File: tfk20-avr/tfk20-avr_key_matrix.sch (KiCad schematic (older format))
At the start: 42 parts

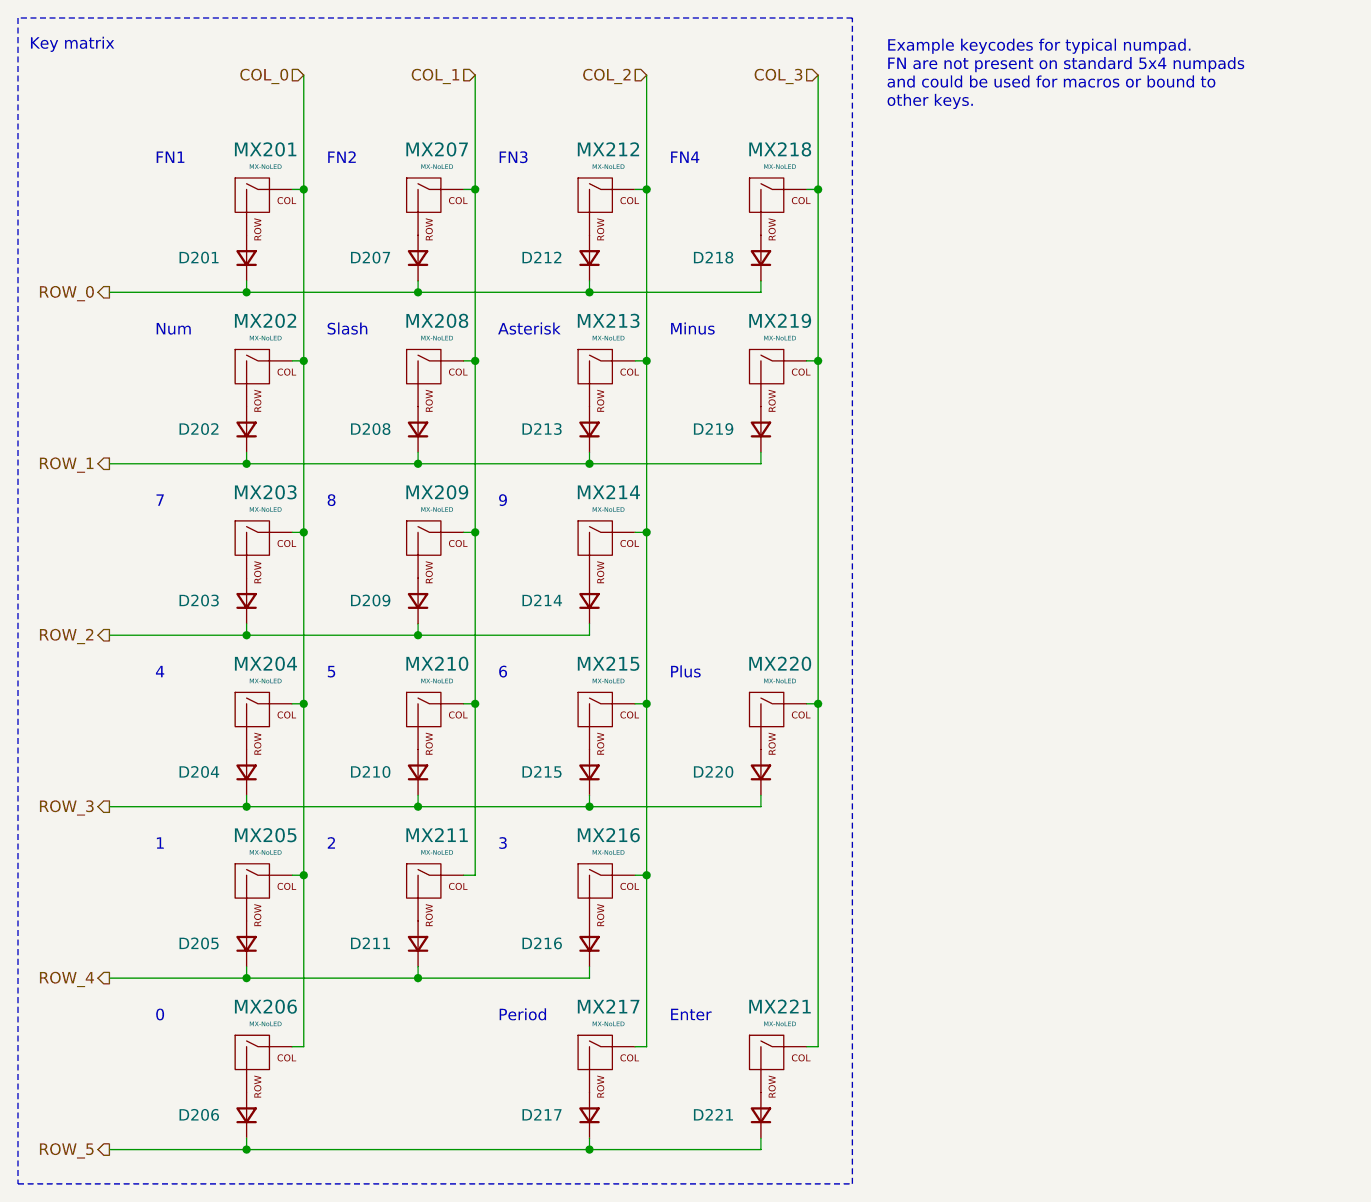
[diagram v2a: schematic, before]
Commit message: Add ISP header
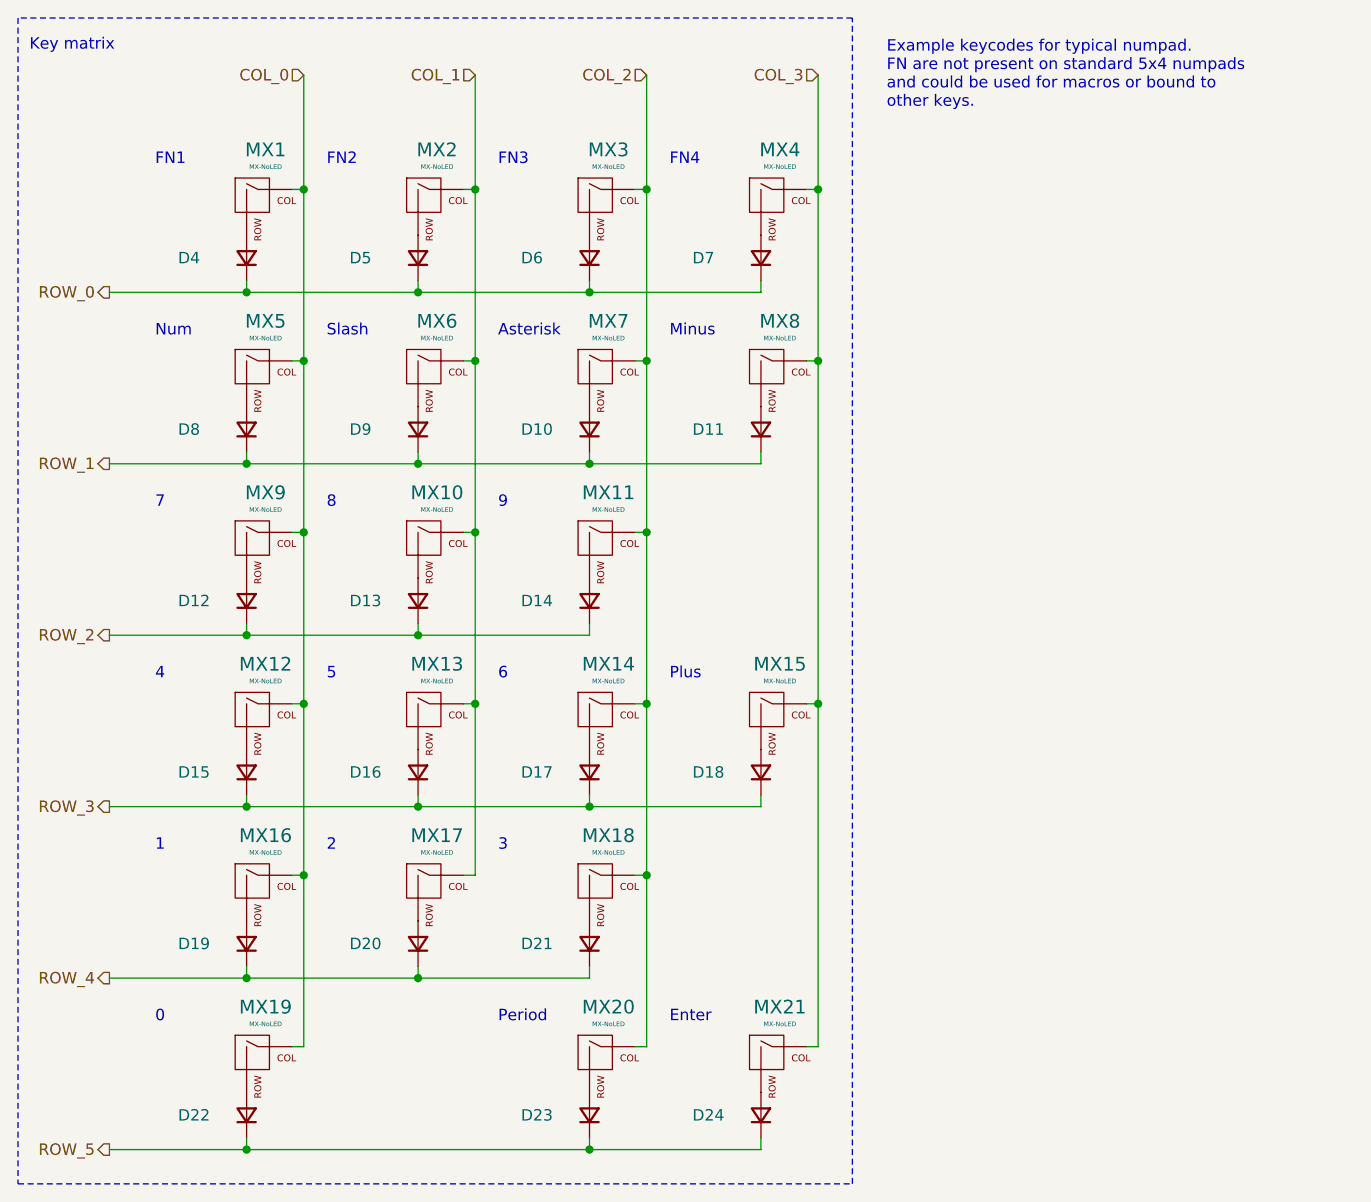
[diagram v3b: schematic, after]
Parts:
- renumbered D213 to D10, D219 to D11, D203 to D12, D209 to D13, D214 to D14, D204 to D15, D210 to D16, D215 to D17, D220 to D18, D205 to D19, D211 to D20, D216 to D21, D206 to D22, D217 to D23, D221 to D24, D201 to D4, D207 to D5, D212 to D6, D218 to D7, D202 to D8, D208 to D9, MX201 to MX1, MX209 to MX10, MX214 to MX11, MX204 to MX12, MX210 to MX13, MX215 to MX14, MX220 to MX15, MX205 to MX16, MX211 to MX17, MX216 to MX18, MX206 to MX19, MX207 to MX2, MX217 to MX20, MX221 to MX21, MX212 to MX3, MX218 to MX4, MX202 to MX5, MX208 to MX6, MX213 to MX7, MX219 to MX8, MX203 to MX9

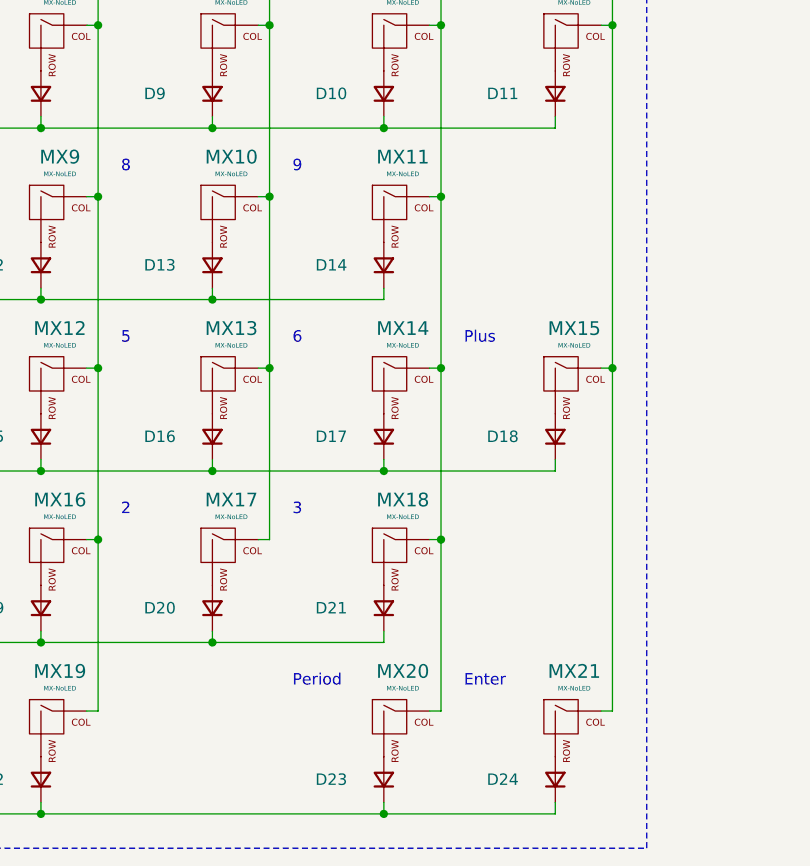
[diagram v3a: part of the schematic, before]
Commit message: Assign some footprints
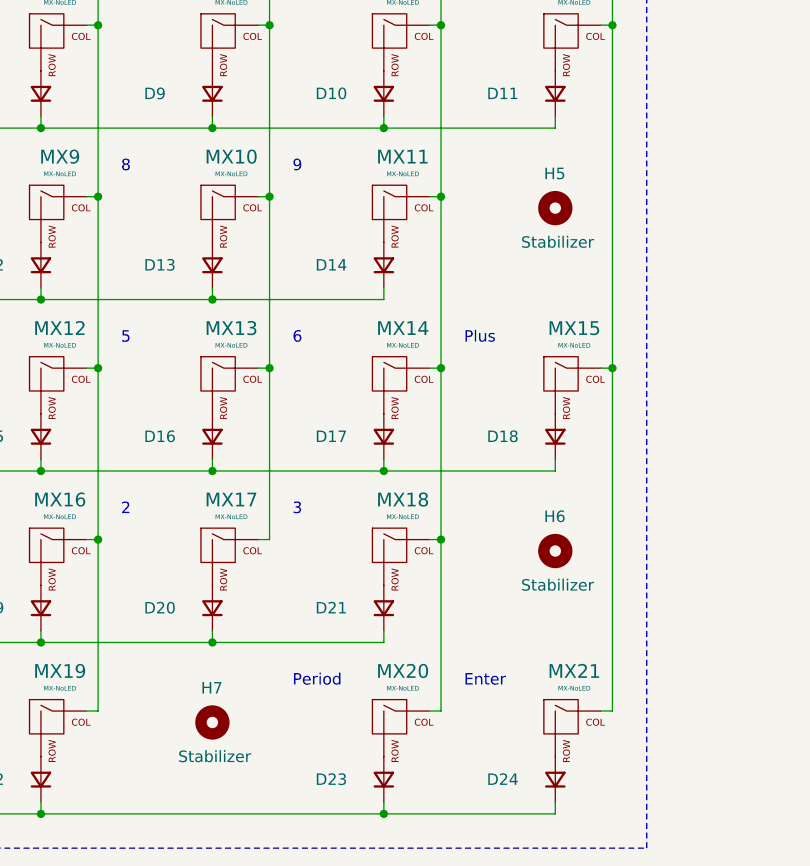
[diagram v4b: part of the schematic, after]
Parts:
- added H5, H6, H7: Stabilizer, Mounting_Keyboard_Stabilizer:Stabilizer_Cherry_MX_2u, symbol Mechanical:MountingHole
- D10, D11, D12, D13, D14, D15, D16, D17, D18, D19, D20, D21, D22, D23, D24, D4, D5, D6, D7, D8, D9: value D_Small -> Switch diode; footprint (none) -> Diode_SMD:D_SOD-123
- MX1, MX10, MX11, MX12, MX13, MX14, MX16, MX17, MX18, MX2, MX20, MX3, MX4, MX5, MX6, MX7, MX8, MX9: footprint (none) -> Switch_Keyboard_Kailh:SW_Hotswap_Kailh_1.00u
- MX15, MX19, MX21: footprint (none) -> Switch_Keyboard_Kailh:SW_Hotswap_Kailh_2.00u

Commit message: Remove alternative LEDs
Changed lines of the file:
@@
 P 4650 2550
 F 0 "MX5" H 4683 2773 60  0000 C CNN
-F 1 "MX-NoLED" H 4683 2699 20  0000 C CNN
+F 1 "MX-NoLED" H 4683 2699 20  0001 C CNN
 F 2 "Switch_Keyboard_Kailh:SW_Hotswap_Kailh_1.00u" H 4025 2525 60  0001 C CNN
 F 3 "" H 4025 2525 60  0001 C CNN
@@
 P 4650 3300
 F 0 "MX9" H 4683 3523 60  0000 C CNN
-F 1 "MX-NoLED" H 4683 3449 20  0000 C CNN
+F 1 "MX-NoLED" H 4683 3449 20  0001 C CNN
 F 2 "Switch_Keyboard_Kailh:SW_Hotswap_Kailh_1.00u" H 4025 3275 60  0001 C CNN
 F 3 "" H 4025 3275 60  0001 C CNN
@@
 P 5400 2550
 F 0 "MX6" H 5433 2773 60  0000 C CNN
-F 1 "MX-NoLED" H 5433 2699 20  0000 C CNN
+F 1 "MX-NoLED" H 5433 2699 20  0001 C CNN
 F 2 "Switch_Keyboard_Kailh:SW_Hotswap_Kailh_1.00u" H 4775 2525 60  0001 C CNN
 F 3 "" H 4775 2525 60  0001 C CNN
@@
 P 5400 3300
 F 0 "MX10" H 5433 3523 60  0000 C CNN
-F 1 "MX-NoLED" H 5433 3449 20  0000 C CNN
+F 1 "MX-NoLED" H 5433 3449 20  0001 C CNN
 F 2 "Switch_Keyboard_Kailh:SW_Hotswap_Kailh_1.00u" H 4775 3275 60  0001 C CNN
 F 3 "" H 4775 3275 60  0001 C CNN
@@
 P 6150 2550
 F 0 "MX7" H 6183 2773 60  0000 C CNN
-F 1 "MX-NoLED" H 6183 2699 20  0000 C CNN
+F 1 "MX-NoLED" H 6183 2699 20  0001 C CNN
 F 2 "Switch_Keyboard_Kailh:SW_Hotswap_Kailh_1.00u" H 5525 2525 60  0001 C CNN
 F 3 "" H 5525 2525 60  0001 C CNN
@@
 P 6150 3300
 F 0 "MX11" H 6183 3523 60  0000 C CNN
-F 1 "MX-NoLED" H 6183 3449 20  0000 C CNN
+F 1 "MX-NoLED" H 6183 3449 20  0001 C CNN
 F 2 "Switch_Keyboard_Kailh:SW_Hotswap_Kailh_1.00u" H 5525 3275 60  0001 C CNN
 F 3 "" H 5525 3275 60  0001 C CNN
@@
 P 6900 2550
 F 0 "MX8" H 6933 2773 60  0000 C CNN
-F 1 "MX-NoLED" H 6933 2699 20  0000 C CNN
+F 1 "MX-NoLED" H 6933 2699 20  0001 C CNN
 F 2 "Switch_Keyboard_Kailh:SW_Hotswap_Kailh_1.00u" H 6275 2525 60  0001 C CNN
 F 3 "" H 6275 2525 60  0001 C CNN
@@
 P 4650 4050
 F 0 "MX12" H 4683 4273 60  0000 C CNN
-F 1 "MX-NoLED" H 4683 4199 20  0000 C CNN
+F 1 "MX-NoLED" H 4683 4199 20  0001 C CNN
 F 2 "Switch_Keyboard_Kailh:SW_Hotswap_Kailh_1.00u" H 4025 4025 60  0001 C CNN
 F 3 "" H 4025 4025 60  0001 C CNN
@@
 P 5400 4050
 F 0 "MX13" H 5433 4273 60  0000 C CNN
-F 1 "MX-NoLED" H 5433 4199 20  0000 C CNN
+F 1 "MX-NoLED" H 5433 4199 20  0001 C CNN
 F 2 "Switch_Keyboard_Kailh:SW_Hotswap_Kailh_1.00u" H 4775 4025 60  0001 C CNN
 F 3 "" H 4775 4025 60  0001 C CNN
@@
 P 6150 4050
 F 0 "MX14" H 6183 4273 60  0000 C CNN
-F 1 "MX-NoLED" H 6183 4199 20  0000 C CNN
+F 1 "MX-NoLED" H 6183 4199 20  0001 C CNN
 F 2 "Switch_Keyboard_Kailh:SW_Hotswap_Kailh_1.00u" H 5525 4025 60  0001 C CNN
 F 3 "" H 5525 4025 60  0001 C CNN
@@
 P 6900 4050
 F 0 "MX15" H 6933 4273 60  0000 C CNN
-F 1 "MX-NoLED" H 6933 4199 20  0000 C CNN
+F 1 "MX-NoLED" H 6933 4199 20  0001 C CNN
 F 2 "Switch_Keyboard_Kailh:SW_Hotswap_Kailh_2.00u" H 6275 4025 60  0001 C CNN
 F 3 "" H 6275 4025 60  0001 C CNN
@@
 P 4650 4800
 F 0 "MX16" H 4683 5023 60  0000 C CNN
-F 1 "MX-NoLED" H 4683 4949 20  0000 C CNN
+F 1 "MX-NoLED" H 4683 4949 20  0001 C CNN
 F 2 "Switch_Keyboard_Kailh:SW_Hotswap_Kailh_1.00u" H 4025 4775 60  0001 C CNN
 F 3 "" H 4025 4775 60  0001 C CNN
@@
 P 5400 4800
 F 0 "MX17" H 5433 5023 60  0000 C CNN
-F 1 "MX-NoLED" H 5433 4949 20  0000 C CNN
+F 1 "MX-NoLED" H 5433 4949 20  0001 C CNN
 F 2 "Switch_Keyboard_Kailh:SW_Hotswap_Kailh_1.00u" H 4775 4775 60  0001 C CNN
 F 3 "" H 4775 4775 60  0001 C CNN
@@
 P 6150 4800
 F 0 "MX18" H 6183 5023 60  0000 C CNN
-F 1 "MX-NoLED" H 6183 4949 20  0000 C CNN
+F 1 "MX-NoLED" H 6183 4949 20  0001 C CNN
 F 2 "Switch_Keyboard_Kailh:SW_Hotswap_Kailh_1.00u" H 5525 4775 60  0001 C CNN
 F 3 "" H 5525 4775 60  0001 C CNN
@@
 P 4650 5550
 F 0 "MX19" H 4683 5773 60  0000 C CNN
-F 1 "MX-NoLED" H 4683 5699 20  0000 C CNN
+F 1 "MX-NoLED" H 4683 5699 20  0001 C CNN
 F 2 "Switch_Keyboard_Kailh:SW_Hotswap_Kailh_2.00u" H 4025 5525 60  0001 C CNN
 F 3 "" H 4025 5525 60  0001 C CNN
@@
 P 6150 5550
 F 0 "MX20" H 6183 5773 60  0000 C CNN
-F 1 "MX-NoLED" H 6183 5699 20  0000 C CNN
+F 1 "MX-NoLED" H 6183 5699 20  0001 C CNN
 F 2 "Switch_Keyboard_Kailh:SW_Hotswap_Kailh_1.00u" H 5525 5525 60  0001 C CNN
 F 3 "" H 5525 5525 60  0001 C CNN
@@
 P 6900 5550
 F 0 "MX21" H 6933 5773 60  0000 C CNN
-F 1 "MX-NoLED" H 6933 5699 20  0000 C CNN
+F 1 "MX-NoLED" H 6933 5699 20  0001 C CNN
 F 2 "Switch_Keyboard_Kailh:SW_Hotswap_Kailh_2.00u" H 6275 5525 60  0001 C CNN
 F 3 "" H 6275 5525 60  0001 C CNN
@@
 P 4650 1800
 F 0 "MX1" H 4683 2023 60  0000 C CNN
-F 1 "MX-NoLED" H 4683 1949 20  0000 C CNN
+F 1 "MX-NoLED" H 4683 1949 20  0001 C CNN
 F 2 "Switch_Keyboard_Kailh:SW_Hotswap_Kailh_1.00u" H 4025 1775 60  0001 C CNN
 F 3 "" H 4025 1775 60  0001 C CNN
@@
 P 5400 1800
 F 0 "MX2" H 5433 2023 60  0000 C CNN
-F 1 "MX-NoLED" H 5433 1949 20  0000 C CNN
+F 1 "MX-NoLED" H 5433 1949 20  0001 C CNN
 F 2 "Switch_Keyboard_Kailh:SW_Hotswap_Kailh_1.00u" H 4775 1775 60  0001 C CNN
 F 3 "" H 4775 1775 60  0001 C CNN
@@
 P 6150 1800
 F 0 "MX3" H 6183 2023 60  0000 C CNN
-F 1 "MX-NoLED" H 6183 1949 20  0000 C CNN
+F 1 "MX-NoLED" H 6183 1949 20  0001 C CNN
 F 2 "Switch_Keyboard_Kailh:SW_Hotswap_Kailh_1.00u" H 5525 1775 60  0001 C CNN
 F 3 "" H 5525 1775 60  0001 C CNN
@@
 P 6900 1800
 F 0 "MX4" H 6933 2023 60  0000 C CNN
-F 1 "MX-NoLED" H 6933 1949 20  0000 C CNN
+F 1 "MX-NoLED" H 6933 1949 20  0001 C CNN
 F 2 "Switch_Keyboard_Kailh:SW_Hotswap_Kailh_1.00u" H 6275 1775 60  0001 C CNN
 F 3 "" H 6275 1775 60  0001 C CNN

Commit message: Route PWR and GND
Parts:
- H5, H6, H7: footprint Mounting_Keyboard_Stabilizer:Stabilizer_Cherry_MX_2u -> Mounting_Keyboard_Stabilizer:Stabilizer_Cherry_MX_2u_CrtYd
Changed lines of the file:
@@
 F 0 "H7" H 5300 5700 50  0000 L CNN
 F 1 "Stabilizer" H 5200 5400 50  0000 L CNN
-F 2 "Mounting_Keyboard_Stabilizer:Stabilizer_Cherry_MX_2u" H 5350 5550 50  0001 C CNN
+F 2 "Mounting_Keyboard_Stabilizer:Stabilizer_Cherry_MX_2u_CrtYd" H 5350 5550 50  0001 C CNN
 F 3 "~" H 5350 5550 50  0001 C CNN
 	1    5350 5550
@@
 F 0 "H6" H 6800 4950 50  0000 L CNN
 F 1 "Stabilizer" H 6700 4650 50  0000 L CNN
-F 2 "Mounting_Keyboard_Stabilizer:Stabilizer_Cherry_MX_2u" H 6850 4800 50  0001 C CNN
+F 2 "Mounting_Keyboard_Stabilizer:Stabilizer_Cherry_MX_2u_CrtYd" H 6850 4800 50  0001 C CNN
 F 3 "~" H 6850 4800 50  0001 C CNN
 	1    6850 4800
@@
 F 0 "H5" H 6800 3450 50  0000 L CNN
 F 1 "Stabilizer" H 6700 3150 50  0000 L CNN
-F 2 "Mounting_Keyboard_Stabilizer:Stabilizer_Cherry_MX_2u" H 6850 3300 50  0001 C CNN
+F 2 "Mounting_Keyboard_Stabilizer:Stabilizer_Cherry_MX_2u_CrtYd" H 6850 3300 50  0001 C CNN
 F 3 "~" H 6850 3300 50  0001 C CNN
 	1    6850 3300
